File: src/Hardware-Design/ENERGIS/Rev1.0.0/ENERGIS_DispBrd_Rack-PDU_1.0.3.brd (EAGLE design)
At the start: 124 x 28 mm, 80 parts, among them CON1 DNI, CON2 AFC11-S20ICC-00, IC1 MCP23017T-E/ML, IC2 MCP23017T-E/ML, T1 BSS138

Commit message: update documentation
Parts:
- removed D1, D2, D3, D4: PTVS3V3S1UR,115, ds_diode:SOD-123
- removed D5: RCLAMP0582BQTCT, ds_diode:SOT-523
- removed R16, R17, R18, R19: 10K 1%, ds_resistor:0402
- R12, R13, R5, R6: value 33K 1% -> 10K 1%
- moved R13 1.40 mm to (106.8, 37.9)
- moved R6 1.00 mm to (63.5, 35.9), turned to 90 degrees
- moved C10 0.71 mm to (106.8, 34.6)
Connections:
- removed net N$24: D3.C, O.3, O.4, R18.1
- removed net N$25: D4.C, PWR.3, PWR.4, R19.1
- removed net N$26: >.3, >.4, D1.C, R17.1
- removed net N$7: <.3, <.4, D2.C, R16.1
- net GND: no longer D1.A, D2.A, D3.A, D4.A, D5.3
- net I2C0_SCL: no longer D5.1
- net I2C0_SDA: no longer D5.2
- net KEY_0: now also <.3, <.4; no longer R16.2
- net KEY_1: now also >.3, >.4; no longer R17.2
- net KEY_2: now also O.3, O.4; no longer R18.2
- net KEY_3: now also PWR.3, PWR.4; no longer R19.2
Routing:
- net GND: track 169.3 -> 123.6 mm, vias 40 -> 37
- net KEY_1: track 17.6 -> 36.2 mm, vias 1 -> 3
- net N$25: track 14.6 -> 0.00 mm
- net N$24: track 14.2 -> 0.00 mm
- net N$7: track 14.1 -> 0.00 mm
- net N$26: track 14.1 -> 0.00 mm, vias 2 -> 0
- net KEY_3: track 64.5 -> 73.4 mm
- net KEY_0: track 40.7 -> 35.8 mm, vias 3 -> 1
- net +3V3: track 200.4 -> 199.2 mm
- net I2C0_SDA: track 111.3 -> 110.7 mm
- net KEY_2: track 22.8 -> 22.2 mm

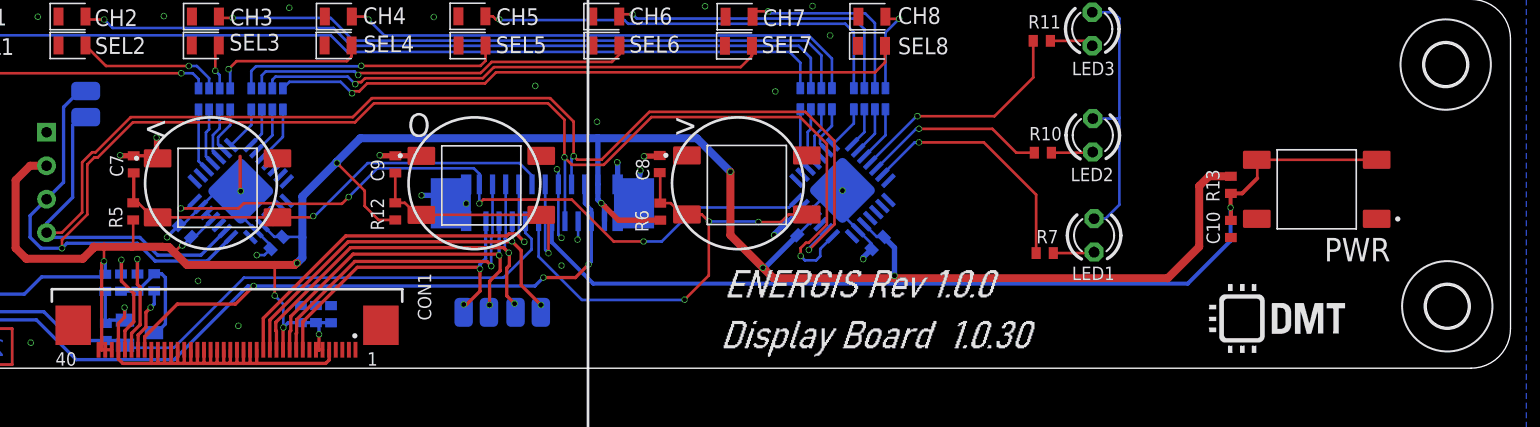
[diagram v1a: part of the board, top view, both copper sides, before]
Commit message: Add software ESD protection to button control and port expanders. Design sheet metal shielding around electronics. Add ethernet test
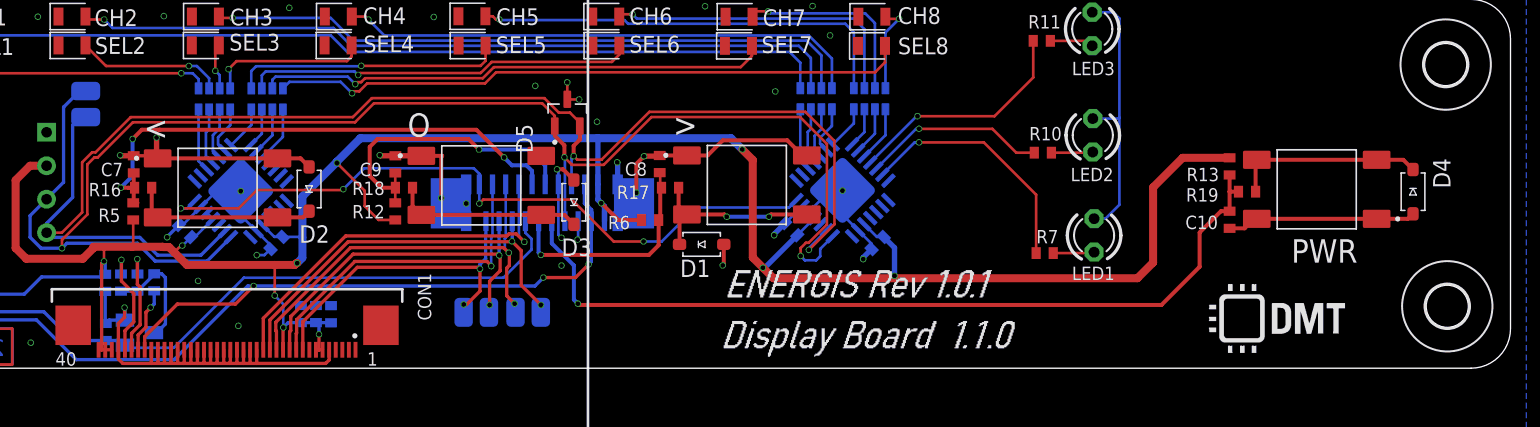
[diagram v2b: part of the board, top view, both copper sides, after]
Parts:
- added D1, D2, D3, D4: PTVS3V3S1UR,115, ds_diode:SOD-123
- added D5: RCLAMP0582BQTCT, ds_diode:SOT-523
- added R16, R17, R18, R19: 10K 1%, ds_resistor:0402
- R12, R13, R5, R6: value 10K 1% -> 33K 1%
- moved R13 1.40 mm to (106.7, 39.3)
- moved R6 1.00 mm to (62.7, 35.2), turned to 0 degrees
- moved C10 0.71 mm to (106.7, 35.3)
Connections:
- new net N$24: D3.C, O.3, O.4, R18.1
- new net N$25: D4.C, PWR.3, PWR.4, R19.1
- new net N$26: >.3, >.4, D1.C, R17.1
- new net N$7: <.3, <.4, D2.C, R16.1
- net GND: now also D1.A, D2.A, D3.A, D4.A, D5.3
- net I2C0_SCL: now also D5.1
- net I2C0_SDA: now also D5.2
- net KEY_0: now also R16.2; no longer <.3, <.4
- net KEY_1: now also R17.2; no longer >.3, >.4
- net KEY_2: now also R18.2; no longer O.3, O.4
- net KEY_3: now also R19.2; no longer PWR.3, PWR.4
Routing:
- net GND: track 123.6 -> 169.3 mm, vias 37 -> 40
- net KEY_1: track 36.2 -> 17.6 mm, vias 3 -> 1
- net N$25: track 0.00 -> 14.6 mm
- net N$24: track 0.00 -> 14.2 mm
- net N$7: track 0.00 -> 14.1 mm
- net N$26: track 0.00 -> 14.1 mm, vias 0 -> 2
- net KEY_3: track 73.4 -> 64.5 mm
- net KEY_0: track 35.8 -> 40.7 mm, vias 1 -> 3
- net +3V3: track 199.2 -> 200.4 mm
- net I2C0_SDA: track 110.7 -> 111.3 mm
- net KEY_2: track 22.2 -> 22.8 mm
